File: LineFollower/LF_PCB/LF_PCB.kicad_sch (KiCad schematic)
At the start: 10 parts, among them J1 5-146282-8, J2 5-146282-8, J3 5-146282-8, U1 NUCLEO-L432KC

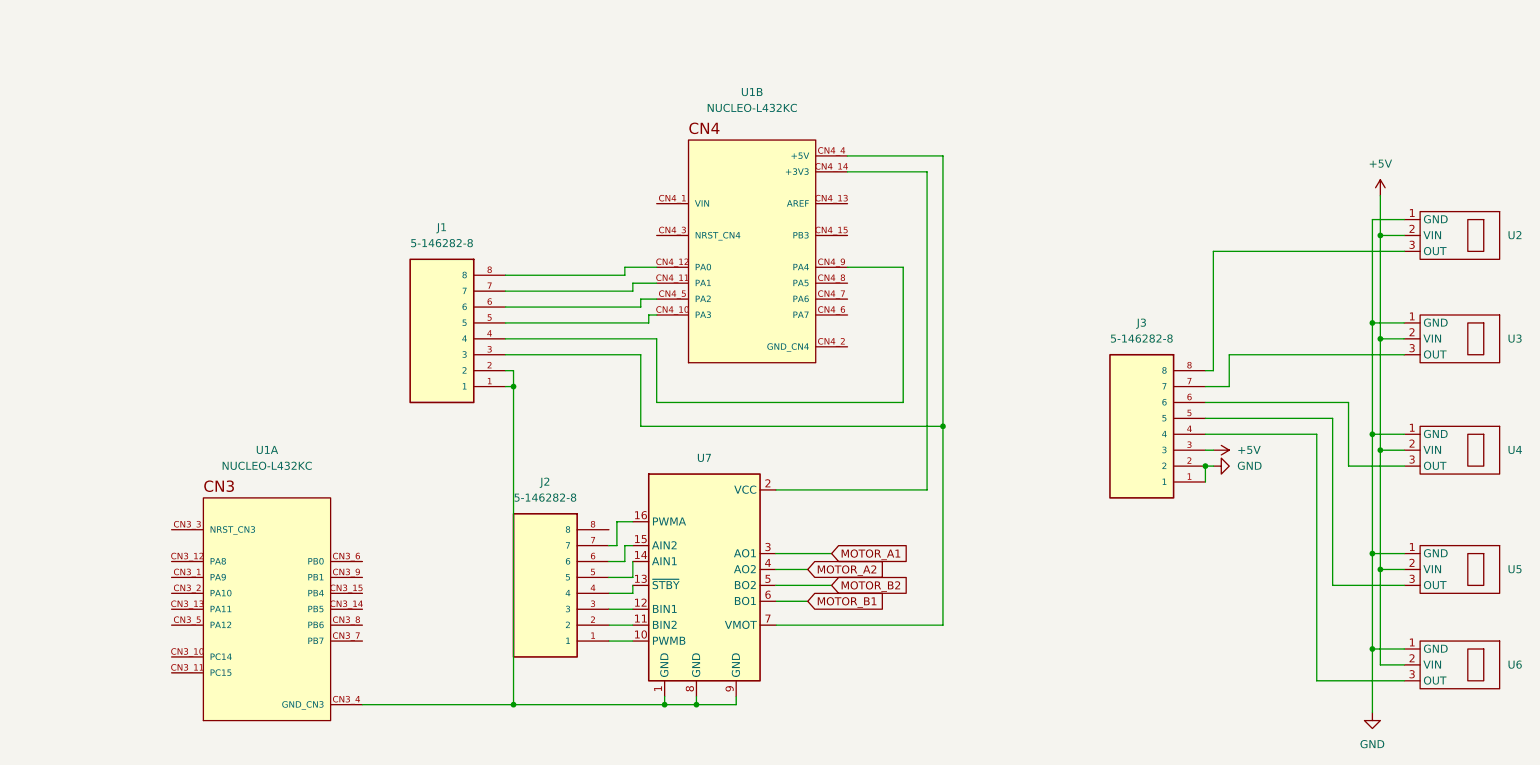
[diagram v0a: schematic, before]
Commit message: push gripper
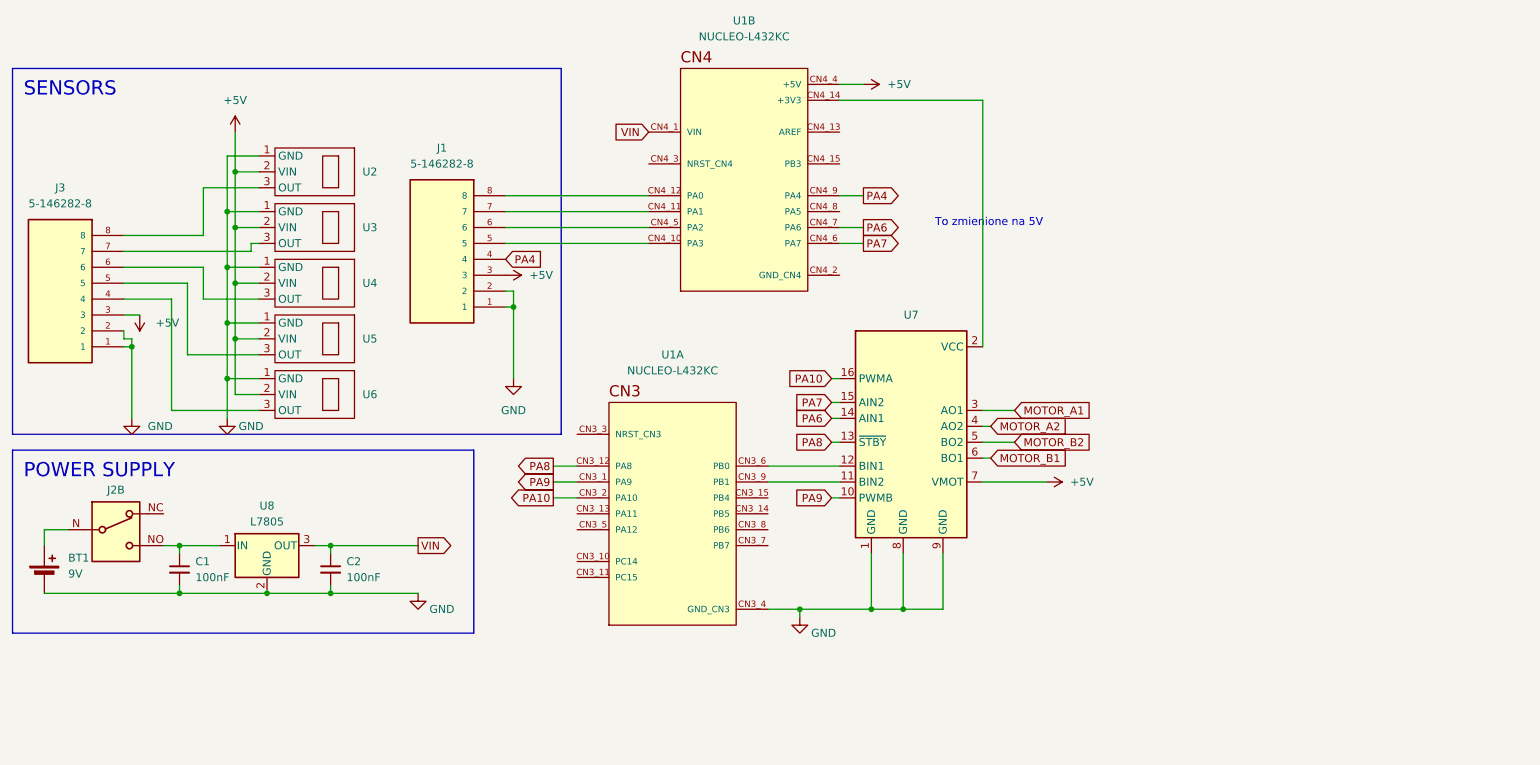
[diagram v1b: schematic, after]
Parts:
- removed J2: 5-146282-8, TE_5-146282-8, symbol 5-146282-8:5-146282-8
- added BT1: 9V, symbol Device:Battery_Cell
- added C1, C2: 100nF, symbol Device:C_Small
- added J2: ~, symbol Connector_Audio:XLR3_Switched
- added U8: L7805, symbol Regulator_Linear:L7805
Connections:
- net +5V: now also J1.3, U1.CN4_4 (+5V), U7.7 (VMOT)
- net GND: now also J1.1, J1.2, U1.CN3_4 (GND_CN3), U7.1 (GND), U7.8 (GND), U7.9 (GND), BT1.2 (-), C1.2, C2.2, U8.2 (GND)
- net PA9: now reaches U7.10 (PWMB)
- net PA9: now also U1.CN3_1 (PA9)
- net at U7.11 (BIN2): now also U1.CN3_9 (PB1)
- net at U7.12 (BIN1): now also U1.CN3_6 (PB0)
- net PA8: now reaches U7.13 (~{STBY})
- net PA8: now also U1.CN3_12 (PA8)
- net PA6: now reaches U7.14 (AIN1)
- net PA6: now also U1.CN4_7 (PA6)
- net PA7: now reaches U7.15 (AIN2)
- net PA7: now also U1.CN4_6 (PA7)
- net PA10: now reaches U7.16 (PWMA)
- net PA10: now also U1.CN3_2 (PA10)
- net VIN: now reaches U1.CN4_1 (VIN)
- net VIN: now also C2.1, U8.3 (OUT)
- net PA4: now reaches J1.4, U1.CN4_9 (PA4)
- new net: BT1.1 (+), J2.N
- new net: C1.1, J2.NO, U8.1 (IN)
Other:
- note added: "To zmienione na 5V"
- moved on the sheet: J1, J3, U1A, U1B, U2, U3, U4, U5, U6, U7
